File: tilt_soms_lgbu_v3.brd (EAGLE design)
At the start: 36 x 90 mm, 40 parts, among them Q1 CMG3415

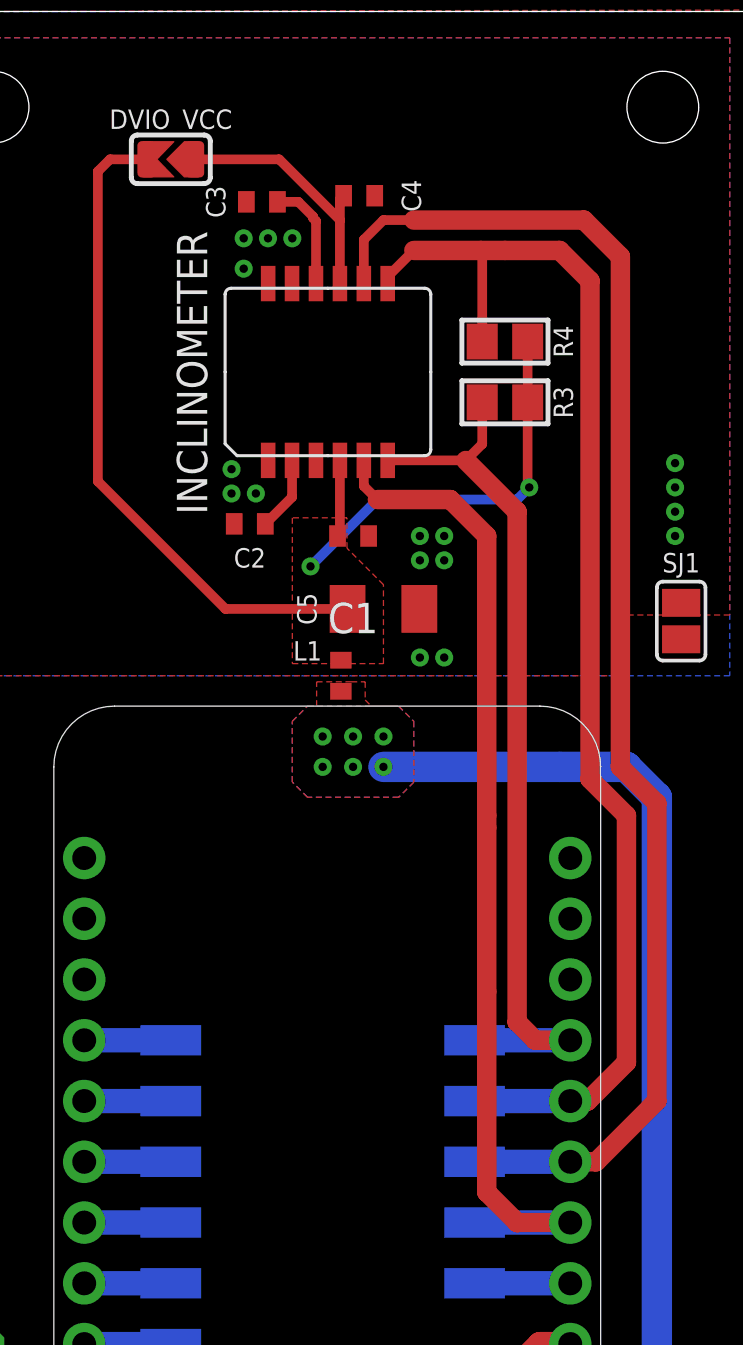
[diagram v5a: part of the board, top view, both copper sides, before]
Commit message: *changed the pad length of scl3300-do1 from 1.48 x 0.61 to 1.96 x 0.61
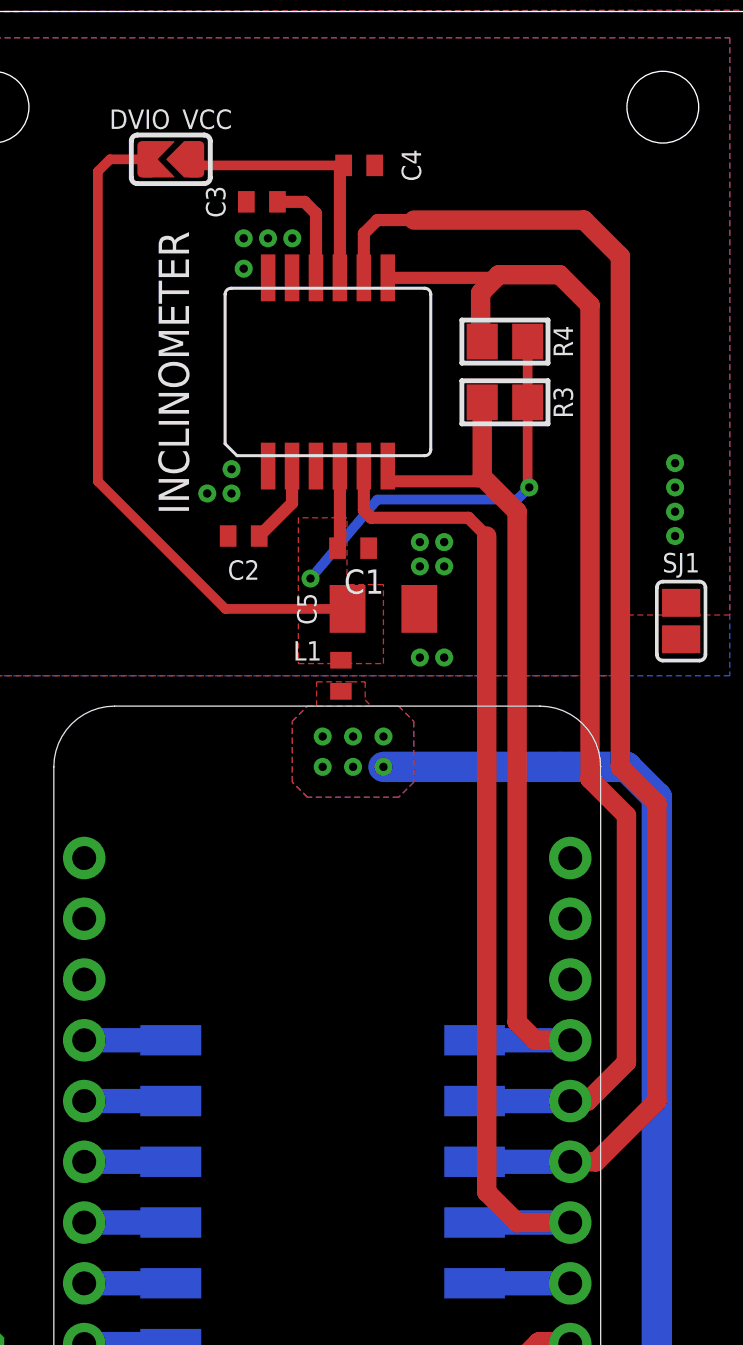
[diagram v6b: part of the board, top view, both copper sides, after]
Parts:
- moved C4 1.27 mm to (19.3, 83.6)
- moved C2 0.57 mm to (14.5, 68.1)
- moved C1 0.51 mm to (19.1, 67.6)
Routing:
- net MISO: track 36.9 -> 40.1 mm
- net MOSI: track 53.9 -> 51.5 mm
- net N$7: track 48.0 -> 48.7 mm

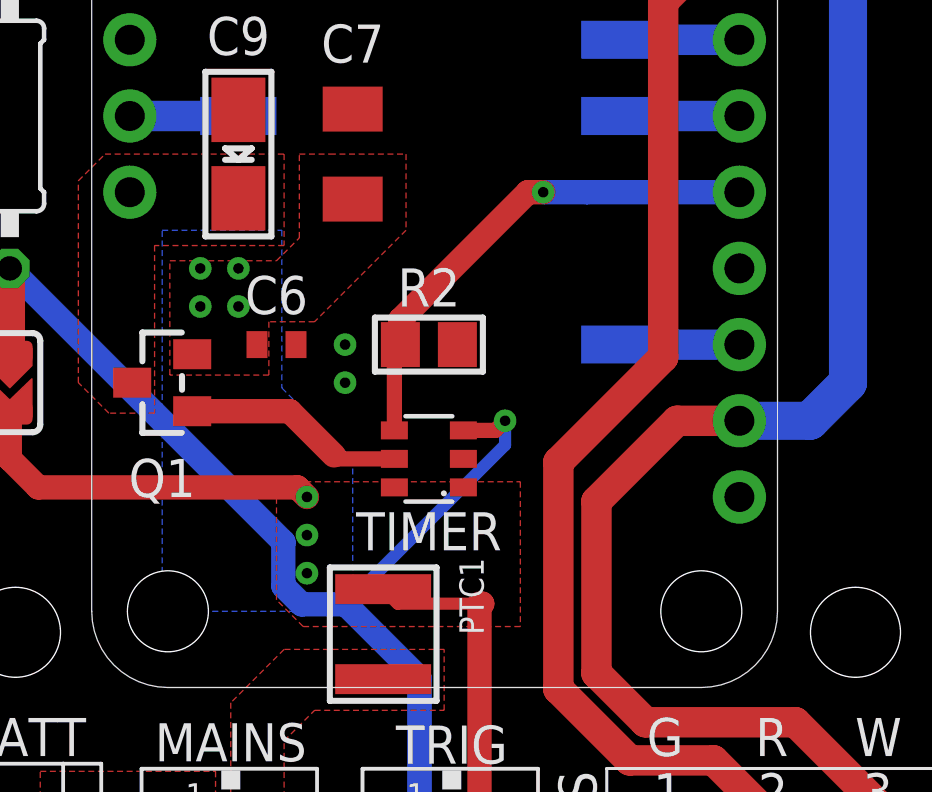
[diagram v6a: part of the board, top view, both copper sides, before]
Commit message: *changed tpl5110 pad length from 0.9 to 1.7
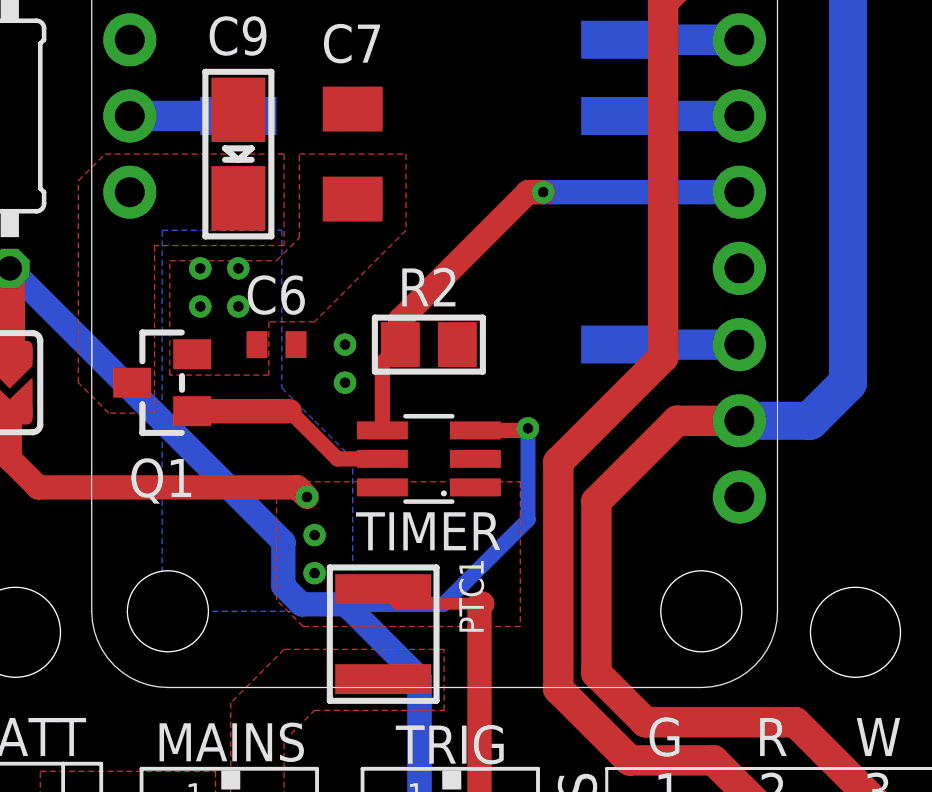
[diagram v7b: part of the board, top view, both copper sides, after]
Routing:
- net DELAY: track 38.0 -> 40.2 mm
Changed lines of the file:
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@@
 <layers>
 <layer number="1" name="Top" color="4" fill="1" visible="yes" active="yes"/>
-<layer number="16" name="Bottom" color="1" fill="1" visible="yes" active="yes"/>
-<layer number="17" name="Pads" color="2" fill="1" visible="yes" active="yes"/>
-<layer number="18" name="Vias" color="2" fill="1" visible="yes" active="yes"/>
-<layer number="19" name="Unrouted" color="6" fill="1" visible="yes" active="yes"/>
-<layer number="20" name="Dimension" color="24" fill="1" visible="yes" active="yes"/>
-<layer number="21" name="tPlace" color="7" fill="1" visible="yes" active="yes"/>
-<layer number="22" name="bPlace" color="7" fill="1" visible="yes" active="yes"/>
-<layer number="23" name="tOrigins" color="15" fill="1" visible="yes" active="yes"/>
+<layer number="16" name="Bottom" color="1" fill="1" visible="no" active="yes"/>
+<layer number="17" name="Pads" color="2" fill="1" visible="no" active="yes"/>
+<layer number="18" name="Vias" color="2" fill="1" visible="no" active="yes"/>
+<layer number="19" name="Unrouted" color="6" fill="1" visible="no" active="yes"/>
+<layer number="20" name="Dimension" color="24" fill="1" visible="no" active="yes"/>
+<layer number="21" name="tPlace" color="7" fill="1" visible="no" active="yes"/>
+<layer number="22" name="bPlace" color="7" fill="1" visible="no" active="yes"/>
+<layer number="23" name="tOrigins" color="15" fill="1" visible="no" active="yes"/>
 <layer number="24" name="bOrigins" color="15" fill="1" visible="no" active="yes"/>
-<layer number="25" name="tNames" color="7" fill="1" visible="yes" active="yes"/>
+<layer number="25" name="tNames" color="7" fill="1" visible="no" active="yes"/>
 <layer number="26" name="bNames" color="7" fill="1" visible="no" active="yes"/>
 <layer number="27" name="tValues" color="7" fill="1" visible="no" active="yes"/>
@@
 <layer number="37" name="tTest" color="7" fill="1" visible="no" active="yes"/>
 <layer number="38" name="bTest" color="7" fill="1" visible="no" active="yes"/>
-<layer number="39" name="tKeepout" color="4" fill="11" visible="yes" active="yes"/>
+<layer number="39" name="tKeepout" color="4" fill="11" visible="no" active="yes"/>
 <layer number="40" name="bKeepout" color="1" fill="11" visible="no" active="yes"/>
-<layer number="41" name="tRestrict" color="4" fill="10" visible="yes" active="yes"/>
+<layer number="41" name="tRestrict" color="4" fill="10" visible="no" active="yes"/>
 <layer number="42" name="bRestrict" color="1" fill="10" visible="no" active="yes"/>
 <layer number="43" name="vRestrict" color="2" fill="10" visible="no" active="yes"/>
 <layer number="44" name="Drills" color="7" fill="1" visible="no" active="yes"/>
-<layer number="45" name="Holes" color="7" fill="1" visible="yes" active="yes"/>
+<layer number="45" name="Holes" color="7" fill="1" visible="no" active="yes"/>
 <layer number="46" name="Milling" color="3" fill="1" visible="no" active="yes"/>
 <layer number="47" name="Measures" color="7" fill="1" visible="no" active="yes"/>
@@
 <layer number="49" name="Reference" color="7" fill="1" visible="no" active="yes"/>
 <layer number="50" name="dxf" color="7" fill="1" visible="no" active="no"/>
-<layer number="51" name="tDocu" color="7" fill="1" visible="yes" active="yes"/>
+<layer number="51" name="tDocu" color="7" fill="1" visible="no" active="yes"/>
 <layer number="52" name="bDocu" color="7" fill="1" visible="no" active="yes"/>
 <layer number="53" name="tGND_GNDA" color="7" fill="9" visible="no" active="no"/>
@@
 <contactref element="TRIG_TEST" pad="1"/>
 <wire x1="3.81" y1="21.336" x2="3.81" y2="24.13" width="1.016" layer="1"/>
-<wire x1="18.93" y1="18.73" x2="20" y2="18.73" width="0.508" layer="1"/>
-<wire x1="20" y1="18.73" x2="20.32" y2="19.05" width="0.508" layer="1"/>
-<via x="20.32" y="19.05" extent="1-16" drill="0.35"/>
+<via x="21.082" y="18.796" extent="1-16" drill="0.35"/>
 <contactref element="TRIG" pad="P1"/>
 <wire x1="17.467" y1="5.2865" x2="17.467" y2="10.473" width="0.8128" layer="16"/>
@@
 <wire x1="15.0086" y1="12.9314" x2="13.53979375" y2="12.9314" width="0.8128" layer="16"/>
 <wire x1="12.9314" y1="13.53979375" x2="12.9314" y2="15.0086" width="0.8128" layer="16"/>
-<wire x1="20.32" y1="19.05" x2="20.32" y2="18.2428" width="0.4064" layer="16"/>
-<wire x1="20.32" y1="18.2428" x2="15.0086" y2="12.9314" width="0.4064" layer="16"/>
+<wire x1="19.33" y1="18.73" x2="21.016" y2="18.73" width="0.508" layer="1"/>
+<wire x1="21.016" y1="18.73" x2="21.082" y2="18.796" width="0.508" layer="1"/>
+<wire x1="15.0086" y1="12.9314" x2="18.2654" y2="12.9314" width="0.508" layer="16"/>
+<wire x1="18.2654" y1="12.9314" x2="21.082" y2="15.748" width="0.508" layer="16"/>
+<wire x1="21.082" y1="15.748" x2="21.082" y2="18.796" width="0.508" layer="16"/>
 </signal>
 <signal name="DONE_PIN">
@@
 <contactref element="TIMER" pad="4"/>
 <contactref element="R2" pad="2"/>
-<wire x1="16.63" y1="18.73" x2="16.63" y2="21.39" width="0.508" layer="1"/>
 <wire x1="16.63" y1="21.39" x2="16.83" y2="21.59" width="0.508" layer="1"/>
-<wire x1="23.0505" y1="26.67" x2="21.59" y2="26.67" width="0.8128" layer="16"/>
 <via x="21.59" y="26.67" extent="1-16" drill="0.35"/>
 <wire x1="16.83" y1="22.418" x2="16.83" y2="21.59" width="0.8128" layer="1"/>
 <wire x1="21.082" y1="26.67" x2="16.83" y2="22.418" width="0.8128" layer="1"/>
-<wire x1="28.1305" y1="26.67" x2="23.0505" y2="26.67" width="0.8128" layer="16"/>
+<wire x1="28.1305" y1="26.67" x2="21.59" y2="26.67" width="0.8128" layer="16"/>
 <wire x1="21.59" y1="26.67" x2="21.082" y2="26.67" width="0.8128" layer="1"/>
+<wire x1="16.23" y1="18.73" x2="16.23" y2="20.99" width="0.508" layer="1"/>
+<wire x1="16.23" y1="20.99" x2="16.83" y2="21.59" width="0.508" layer="1"/>
 </signal>
 <signal name="EN">
@@
 <contactref element="TIMER" pad="5"/>
 <contactref element="Q1" pad="1"/>
-<wire x1="9.89" y1="19.37" x2="13.142" y2="19.37" width="0.8128" layer="1"/>
-<wire x1="14.6152" y1="17.8968" x2="13.142" y2="19.37" width="0.8128" layer="1"/>
-<wire x1="16.63" y1="17.78" x2="14.732" y2="17.78" width="0.508" layer="1"/>
-<wire x1="14.732" y1="17.78" x2="14.6152" y2="17.8968" width="0.508" layer="1"/>
+<wire x1="13.142" y1="19.37" x2="9.89" y2="19.37" width="0.8128" layer="1"/>
+<wire x1="16.23" y1="17.78" x2="14.732" y2="17.78" width="0.508" layer="1"/>
+<wire x1="14.732" y1="17.78" x2="13.142" y2="19.37" width="0.508" layer="1"/>
 </signal>
 <signal name="VBAT">
@@
 <via x="11.43" y="22.86" extent="1-16" drill="0.35"/>
 <via x="13.716" y="16.51" extent="1-16" drill="0.35"/>
-<via x="13.716" y="15.24" extent="1-16" drill="0.35"/>
-<via x="13.716" y="13.97" extent="1-16" drill="0.35"/>
+<via x="13.97" y="15.24" extent="1-16" drill="0.35"/>
+<via x="13.97" y="13.97" extent="1-16" drill="0.35"/>
 <polygon width="0.254" layer="16">
 <vertex x="8.89" y="25.4"/>
@@
 <wire x1="18.5" y1="70.995" x2="18.5" y2="67.664" width="0.508" layer="1"/>
 <wire x1="18.5" y1="67.664" x2="18.4" y2="67.564" width="0.508" layer="1"/>
-<wire x1="18.4" y1="67.564" x2="17.272" y2="66.294" width="0" layer="19" extent="1-16"/>
-<wire x1="18.82" y1="65.024" x2="17.272" y2="66.294" width="0" layer="19" extent="1-16"/>
-<wire x1="18.542" y1="62.88" x2="18.82" y2="65.024" width="0" layer="19" extent="1-1"/>
 </signal>
 <signal name="DGND">
@@
 </signal>
 </signals>
+<errors>
+</errors>
 </board>
 </drawing>
